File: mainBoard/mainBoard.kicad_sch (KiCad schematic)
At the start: 0 parts

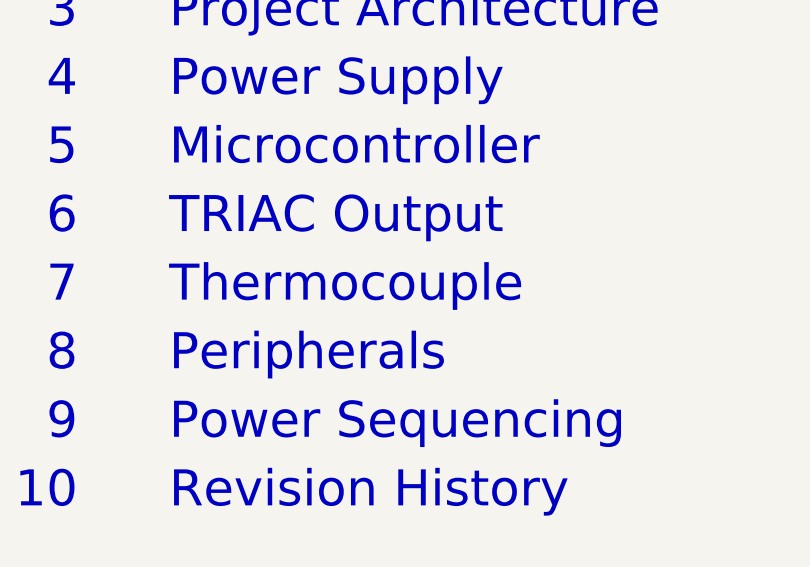
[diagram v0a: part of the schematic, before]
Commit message: tweak schematic for changes from 6-17-2026
major structural changes, see daily note from obsidian
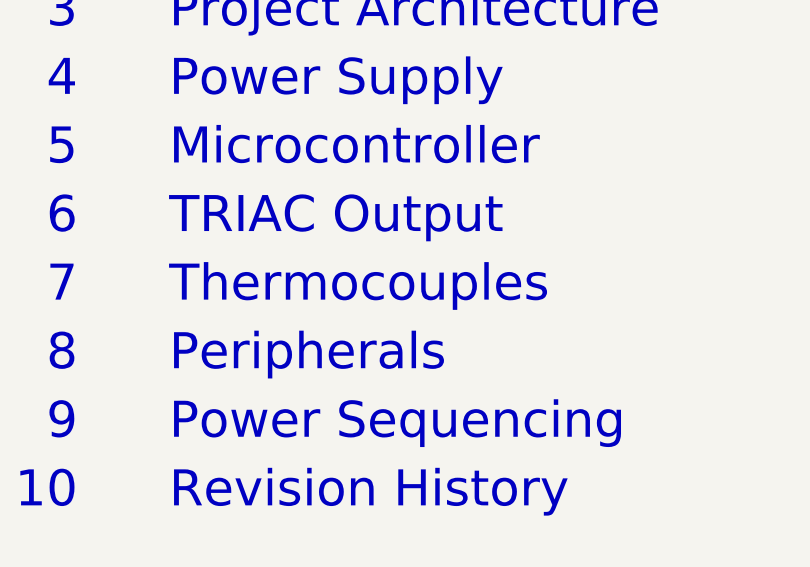
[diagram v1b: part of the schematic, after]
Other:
- note added: "Thermocouples"
- note removed: "Thermocouple"
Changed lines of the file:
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@@
 		)
 	)
-	(text "Thermocouple"
+	(text "Thermocouples"
 		(exclude_from_sim no)
 		(at 45.72 129.54 0)

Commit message: 3d models added to PCB
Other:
- removed sheet Power - Sequencing
- note removed: "BOTTOM VIEW"
- note removed: "Power Sequencing"
